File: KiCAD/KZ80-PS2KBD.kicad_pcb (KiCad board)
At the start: 2 copper layers, 100 x 75 mm, 23 parts, among them J1 232C(DEBUG), J2 PS/2 KB, J3 SBC8080 BUS, J4 ADR-JP2, J5 ADR-JP1, J6 ICSP, J7 CON-A, U1 74HC139, U2 74HC00, U3 8255, U4 ATmega328P-PU

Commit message: REV1基板製造用ガーバーデータ出力版
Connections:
- J1 pad 4: TxD -> RxD
- J1 pad 5: RxD -> TxD
- J3 pad 21: Net-(J3-Pad21) -> RESET
- J3 pad 23: RESET -> Net-(J3-Pad23)
- J6 pad 5: RESET -> /~RESET
- R1 pad 2: RESET -> /~RESET
- U2 pad 5: RESET -> /~RESET
- U4 pad 2: TxD -> RxD
- U4 pad 3: RxD -> TxD
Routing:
- net /~RESET: track 0.00 -> 43.3 mm
- net PPI-CE: track 89.6 -> 120.4 mm
- net TxD: track 79.1 -> 58.7 mm
- net /A7: track 63.4 -> 83.3 mm
- net Net-(U3-Pad14): track 46.1 -> 63.6 mm
- net Net-(U2-Pad3): track 73.0 -> 55.7 mm
- net RESET: track 103.7 -> 89.1 mm
- net RxD: track 53.6 -> 67.8 mm
- net /MISO: track 59.3 -> 71.9 mm
- net VCC: track 257.8 -> 269.4 mm
- net Net-(J4-Pad3): track 22.6 -> 11.6 mm
- net A1: track 56.3 -> 65.7 mm
- net /PA6: track 35.9 -> 26.8 mm
- net ~IOWR: track 37.9 -> 28.7 mm
- net /D6: track 43.9 -> 52.8 mm
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
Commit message: 74HC00 電源ピン配線見直しプリントパターン作成
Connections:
- U2 pad 14: GND -> VCC
- U2 pad 7: VCC -> GND
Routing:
- net PPI-CE: track 120.4 -> 76.8 mm
- net VCC: track 269.4 -> 240.3 mm
- net /A7: track 83.3 -> 60.2 mm
- net A0: track 59.9 -> 81.3 mm
- net Net-(JP1-Pad2): track 26.9 -> 47.7 mm
- net RESET: track 89.1 -> 107.4 mm
- net Net-(U3-Pad14): track 63.6 -> 46.1 mm
- net /MOSI: track 60.1 -> 72.4 mm
- net /MISO: track 71.9 -> 59.7 mm
- net /D4: track 46.6 -> 37.9 mm
- net /D6: track 52.8 -> 44.2 mm
- net /~RESET: track 43.3 -> 51.2 mm
- net Net-(J5-Pad5): track 34.5 -> 28.8 mm
- net TxD: track 58.7 -> 53.6 mm
- net /PA4: track 28.0 -> 23.4 mm
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
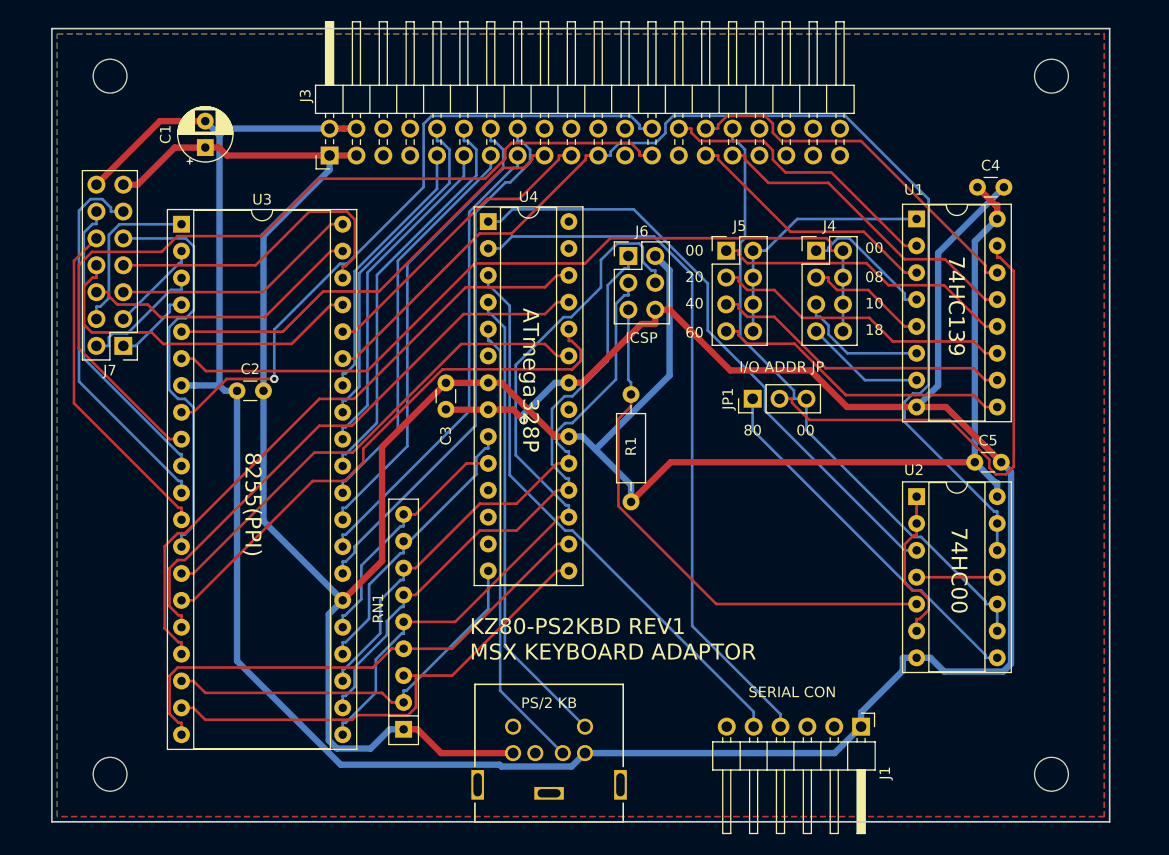
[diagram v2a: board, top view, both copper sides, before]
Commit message: CMT出力回路追加・REV2基板ガーバー出力
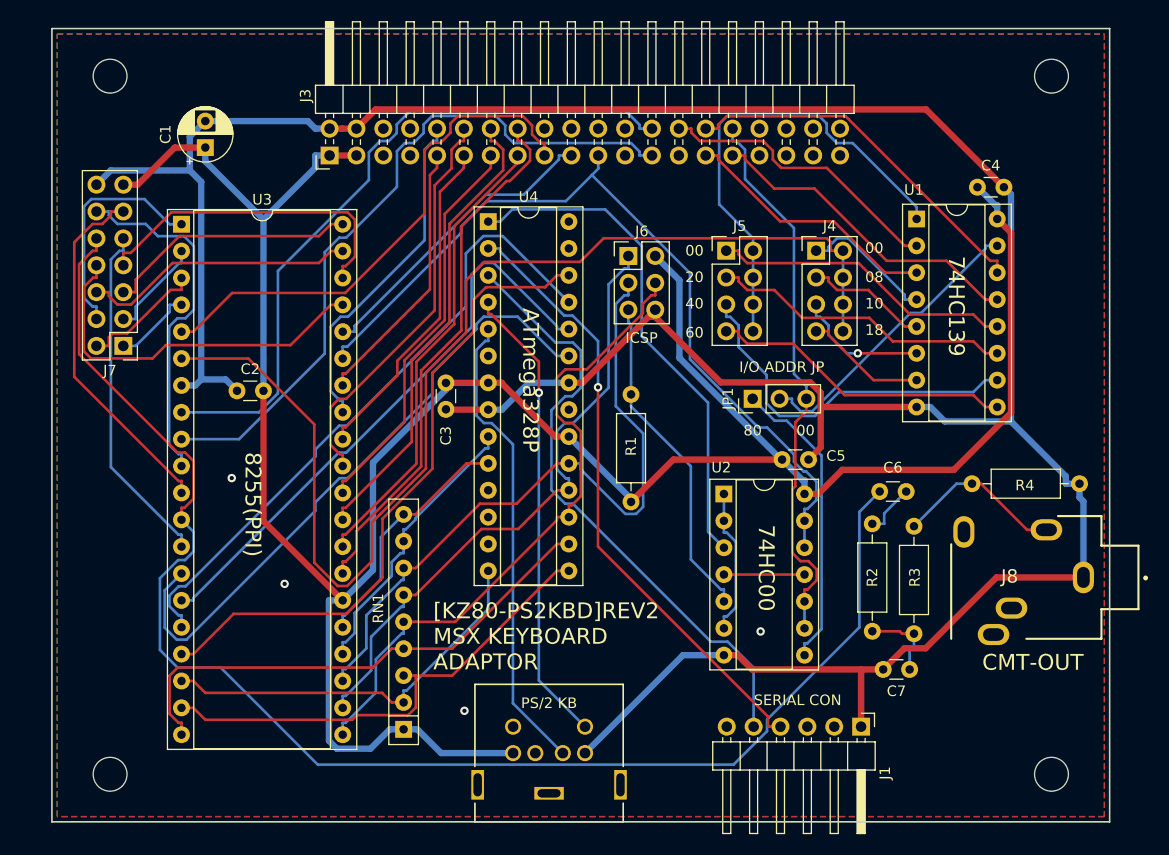
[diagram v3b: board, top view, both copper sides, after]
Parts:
- added C6: 0.1u, Capacitor_THT:C_Disc_D3.0mm_W1.6mm_P2.50mm, F.Cu at (140.8, 93.8)
- added C7: 0.0022u, Capacitor_THT:C_Disc_D3.0mm_W1.6mm_P2.50mm, F.Cu at (141.1, 110.6)
- added J8: CMT-OUT, AJ-1780:AJ-1780, F.Cu at (159.2, 101.9)
- added R2: 4.7k, Resistor_THT:R_Axial_DIN0207_L6.3mm_D2.5mm_P10.16mm_Horizontal, F.Cu at (137.6, 107.0)
- added R3: 47k, Resistor_THT:R_Axial_DIN0207_L6.3mm_D2.5mm_P10.16mm_Horizontal, F.Cu at (141.5, 97.0)
- added R4: 100, Resistor_THT:R_Axial_DIN0207_L6.3mm_D2.5mm_P10.16mm_Horizontal, F.Cu at (147.0, 93.0)
- moved C5 18.2 mm to (129.0, 90.8)
- moved U2 18.2 mm to (123.5, 94.0)
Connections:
- J1 pad 2: Net-(J1-Pad2) -> (no net)
- J1 pad 3: Net-(J1-Pad3) -> (no net)
- J1 pad 6: Net-(J1-Pad6) -> (no net)
- J2 pad 2: Net-(J2-Pad2) -> (no net)
- J2 pad 6: Net-(J2-Pad6) -> (no net)
- J3 pad 18: Net-(J3-Pad18) -> (no net)
- J3 pad 20: Net-(J3-Pad20) -> (no net)
- J3 pad 22: Net-(J3-Pad22) -> (no net)
- J3 pad 23: Net-(J3-Pad23) -> (no net)
- J3 pad 24: Net-(J3-Pad24) -> (no net)
- J3 pad 27: Net-(J3-Pad27) -> (no net)
- J3 pad 33: Net-(J3-Pad33) -> (no net)
- J3 pad 34: Net-(J3-Pad34) -> (no net)
- J3 pad 35: Net-(J3-Pad35) -> (no net)
- J3 pad 36: Net-(J3-Pad36) -> (no net)
- J3 pad 37: Net-(J3-Pad37) -> (no net)
- J3 pad 38: Net-(J3-Pad38) -> (no net)
- J3 pad 39: Net-(J3-Pad39) -> (no net)
- J3 pad 40: Net-(J3-Pad40) -> (no net)
- J3 pad 5: Net-(J3-Pad5) -> (no net)
- J3 pad 6: Net-(J3-Pad6) -> (no net)
- J3 pad 7: Net-(J3-Pad7) -> (no net)
- J3 pad 8: Net-(J3-Pad8) -> (no net)
- U4 pad 11: Net-(U4-Pad11) -> (no net)
- U4 pad 12: Net-(U4-Pad12) -> (no net)
- U4 pad 13: Net-(U4-Pad13) -> (no net)
- U4 pad 21: Net-(U4-Pad21) -> (no net)
- U4 pad 27: Net-(U4-Pad27) -> (no net)
- U4 pad 28: Net-(U4-Pad28) -> (no net)
- U4 pad 6: Net-(U4-Pad6) -> (no net)
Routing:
- net /PC5: track 31.9 -> 137.8 mm
- net PPI-CE: track 76.8 -> 111.6 mm
- net RESET: track 107.4 -> 79.1 mm
- net Net-(J5-Pad2): track 24.6 -> 45.1 mm
- net Net-(JP1-Pad2): track 47.7 -> 27.9 mm
- net /~RESET: track 51.2 -> 31.5 mm
- net Net-(J8-Pad5): track 0.00 -> 16.0 mm
- net GND: track 274.4 -> 289.8 mm, vias 1 -> 4
- net Net-(U3-Pad14): track 46.1 -> 60.5 mm
- net A0: track 81.3 -> 67.5 mm
- net /SCK: track 54.2 -> 65.6 mm
- net Net-(U2-Pad3): track 58.2 -> 48.2 mm
- net /MOSI: track 72.4 -> 62.6 mm
- net RxD: track 67.4 -> 58.5 mm, vias 0 -> 1
- net ~IORD: track 41.4 -> 49.5 mm
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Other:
- board text added: "CMT-OUT"
- board text added: "[KZ80-PS2KBD]REV2 MSX KEYBOARD ADAPTOR"
- board text removed: "KZ80-PS2KBD REV1 MSX KEYBOARD ADAPTOR"

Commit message: REV2基板 部品配置見直し・ガーバーデータ出力
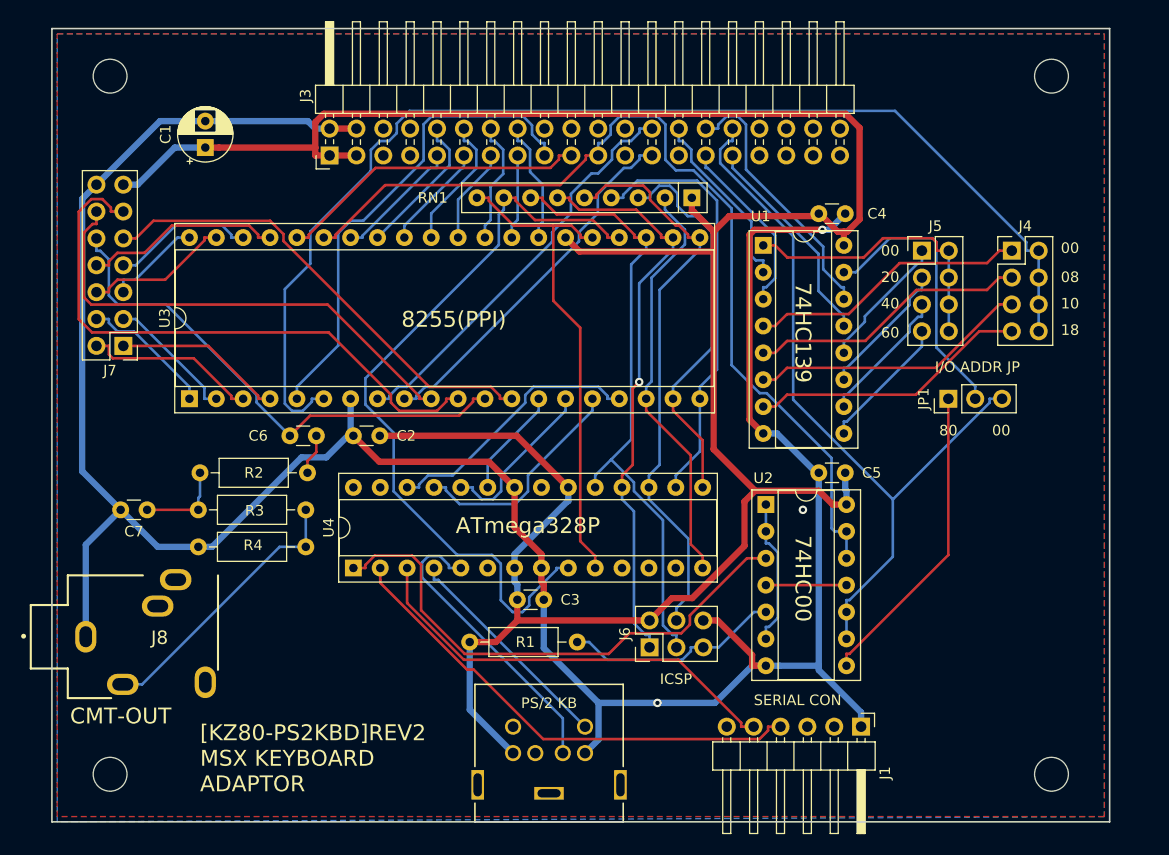
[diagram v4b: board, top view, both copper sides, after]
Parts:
- moved J8 97.9 mm to (61.5, 107.5), turned to 0 degrees
- moved C7 73.7 mm to (69.0, 95.5)
- moved R2 65.3 mm to (74.0, 92.0), turned to 0 degrees
- moved R4 63.3 mm to (84.0, 99.0), turned to 180 degrees
- moved R3 57.5 mm to (84.0, 95.5), turned to 180 degrees
- moved RN1 57.2 mm to (120.5, 66.0), turned to 180 degrees
- moved C6 56.0 mm to (85.0, 88.5)
- moved J6 37.1 mm to (116.5, 108.5), turned to 90 degrees
- moved U4 35.1 mm to (88.5, 101.0), turned to 90 degrees
- moved C3 21.6 mm to (104.0, 104.0), turned to 0 degrees
- moved R1 20.2 mm to (99.5, 108.0), turned to 0 degrees
- moved J4 18.5 mm to (150.8, 71.0)
- moved J5 18.5 mm to (142.2, 71.0)
- moved JP1 18.5 mm to (144.8, 85.0)
- moved U3 16.5 mm to (73.0, 85.0), turned to 90 degrees
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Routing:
- net /PC5: track 137.8 -> 49.2 mm
- net Net-(U3-Pad14): track 60.5 -> 10.4 mm
- net GND: track 289.8 -> 243.2 mm, vias 4 -> 3
- net Net-(RN1-Pad8): track 26.9 -> 72.6 mm
- net Net-(U3-Pad16): track 61.4 -> 21.5 mm
- net Net-(U3-Pad15): track 55.7 -> 16.0 mm
- net /D7: track 50.4 -> 11.7 mm
- net Net-(U3-Pad17): track 61.8 -> 25.2 mm
- net /D6: track 44.0 -> 7.99 mm
- net A0: track 67.5 -> 34.9 mm
- net /D5: track 44.1 -> 11.7 mm
- net /D4: track 37.9 -> 9.10 mm
- net A1: track 66.0 -> 39.0 mm
- net /D3: track 38.4 -> 12.8 mm
- net Net-(RN1-Pad9): track 23.2 -> 46.8 mm
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
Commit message: プリントパターン見直し・ガーバーデータ再出力
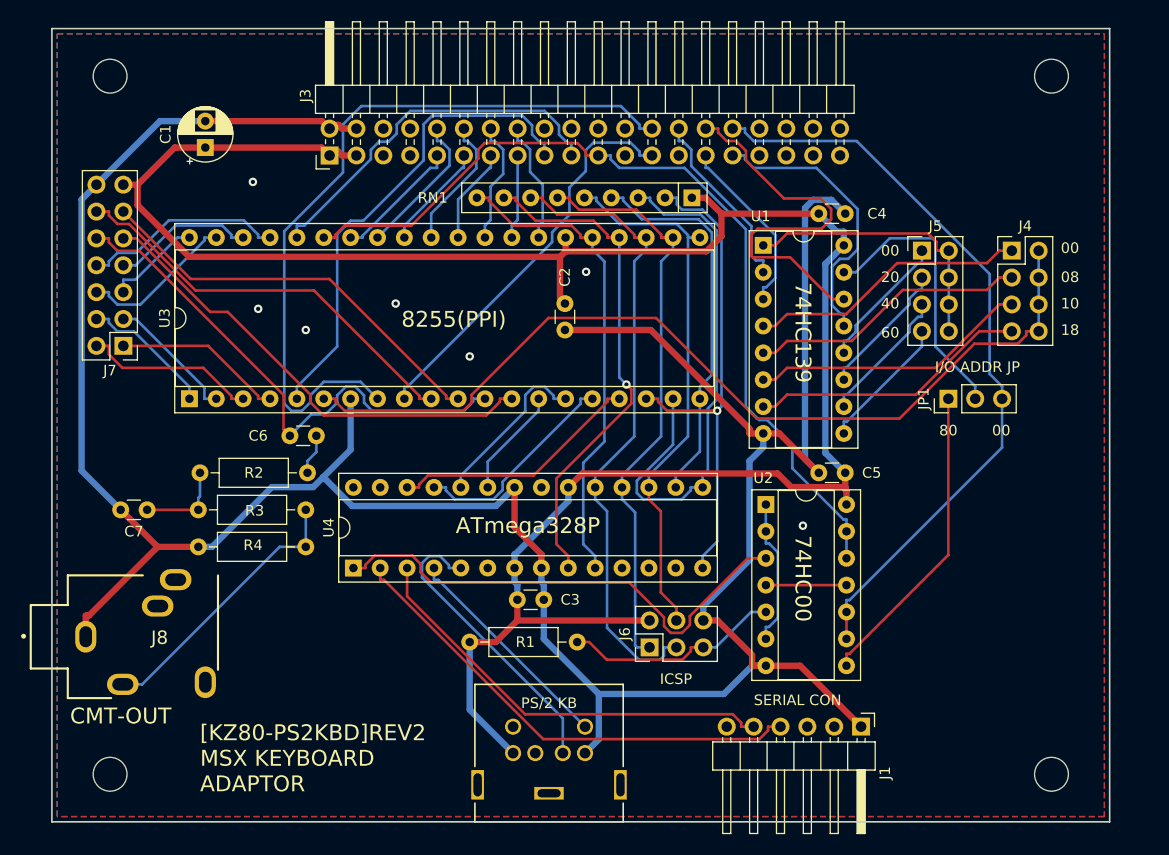
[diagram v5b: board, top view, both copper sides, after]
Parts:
- moved C2 22.4 mm to (108.5, 78.5), turned to 90 degrees
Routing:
- net VCC: track 243.9 -> 207.5 mm
- net A1: track 39.0 -> 71.0 mm
- net GND: track 243.2 -> 269.6 mm, vias 3 -> 7
- net Net-(RN1-Pad8): track 72.6 -> 47.9 mm, vias 0 -> 1
- net PPI-CE: track 110.7 -> 87.5 mm
- net /PC6: track 56.1 -> 39.1 mm
- net Net-(RN1-Pad3): track 36.9 -> 51.1 mm
- net /A5: track 25.3 -> 37.3 mm
- net Net-(RN1-Pad2): track 39.5 -> 47.1 mm, vias 0 -> 1
- net /A6: track 20.6 -> 27.3 mm
- net /PC7: track 45.7 -> 39.4 mm
- net ~IOWR: track 29.5 -> 35.5 mm
- net RESET: track 89.1 -> 83.8 mm
- net Net-(RN1-Pad4): track 40.3 -> 36.5 mm
- net Net-(U2-Pad3): track 50.3 -> 47.0 mm
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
